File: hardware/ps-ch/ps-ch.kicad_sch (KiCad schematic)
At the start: 67 parts, among them Q11 MMBT3904, U10 ADuM1401xRW, U11 LMR51610X, U13 ADuM1401xRW, U3 LM61495, U5 OPA992IDCKR

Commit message: - added component values/part numbers
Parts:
- removed C24, C33, C41, C50, C51, C52, C53, C57, C61: C, symbol Device:C
- removed R20: R, symbol Device:R
- added C24, C50, C52, C53, C57, C81: 0.1μF 0603 100Vdc X7R ±20%, Capacitor_SMD:C_0603_1608Metric, symbol ps-ch:0.1μF 0603 100Vdc X7R ±20%
- added C33, C41: 10μF 0805 50Vdc X5R ±20%, Capacitor_SMD:C_0805_2012Metric, symbol ps-ch:10μF 0805 50Vdc X5R ±20%
- added C51, C61: 10μF 1210 100Vdc X7S ±20%, Capacitor_SMD:C_1210_3225Metric, symbol ps-ch:10μF 1210 100Vdc X7S ±20%
- C12, C20, C21, C22: value C -> 10μF 1210 100Vdc X7S ±20%; footprint (none) -> Capacitor_SMD:C_1210_3225Metric; symbol Device:C -> ps-ch:10μF 1210 100Vdc X7S ±20%; DisplayValue0 (none) -> 10μF ±20%; DisplayValue1 (none) -> 1210 100Vdc; DisplayValue2 (none) -> X7S; Manufacturer (none) -> Murata; Manufacturer Part Number (none) -> GRM188R72A104MA35
- C14, C19, C23, C34, C46, C47, C48, C56: value C -> 0.1μF 0603 100Vdc X7R ±20%; footprint (none) -> Capacitor_SMD:C_0603_1608Metric; symbol Device:C -> ps-ch:0.1μF 0603 100Vdc X7R ±20%; DisplayValue0 (none) -> 0.1μF ±20%; DisplayValue1 (none) -> 0603 100Vdc; DisplayValue2 (none) -> X7R; Manufacturer (none) -> Murata; Manufacturer Part Number (none) -> GRM188R72A104MA35
- L4: value L -> 60Ω@100MHz; footprint (none) -> Inductor_SMD:L_0603_1608Metric; symbol Device:L -> ps-ch:74437349015; Manufacturer (none) -> Wuerth Elektronik; Manufacturer Part Number (none) -> 74279228600
- R50, R56, R63, R67: value R -> 10kΩ 0603 0.1W ±1% ±100ppm/°C; footprint (none) -> Resistor_SMD:R_0603_1608Metric; symbol Device:R -> ps-ch:10kΩ 0603 0.1W ±1% ±100ppm/°C; DisplayValue0 (none) -> 10kΩ ±1%; DisplayValue1 (none) -> 0603 0.1W; DisplayValue2 (none) -> ±100ppm; Manufacturer (none) -> Yageo; Manufacturer Part Number (none) -> AC0603FR-0710KL
- R57, R58: value R -> 22Ω 0402 0.063W ±1% ±100ppm/°C; footprint (none) -> Resistor_SMD:R_0402_1005Metric; symbol Device:R -> ps-ch:22Ω 0402 0.063W ±1% ±100ppm/°C; DisplayValue0 (none) -> 22Ω ±1%; DisplayValue1 (none) -> 0402 0.063W; DisplayValue2 (none) -> ±100ppm; Manufacturer (none) -> Yageo; Manufacturer Part Number (none) -> AC0402FR-0722RL
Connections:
- net +3V3: now also C19.2, C46.2, R50.1, C52.2, C53.2, C57.2, C81.2; no longer C19.1, C46.1, R50.2
- net 3V3: now also C47.2, C56.2, R56.2; no longer C47.1, C56.1, R56.1
- net ACTIVATE_BOOTLOADER: now also R63.2; no longer R63.1
- net ARM_OUTPUT: now also R67.2; no longer R67.1
- net Earth: now also C47.1, C56.1, R63.1, R67.1; no longer C47.2, C56.2, R63.2, R67.2
- net Flyback Converter/V_PREREG_EQUIV_PWM: now also U10.14 (VOA)
- net GND: now also C12.1, C19.1, C20.1, C21.1, C22.1, C23.1, C34.1, C46.1, C24.1, C33.1, C41.1, C50.1, C51.1, C52.1, C53.1, C57.1, C61.1, C81.1; no longer C12.2, C19.2, C20.2, C21.2, C22.2, C23.2, C34.2, C46.2
- net NRST: now also R56.1; no longer R56.2
- net PG: now also R50.2; no longer R50.1
- net STM32/STM32_UART_RX: now also R58.2; no longer R58.1
- net UART_RX: now also R57.1; no longer R57.2
- net VDC: now also L4.2, C41.2, C61.2; no longer L4.1
- net at L2.1, U3.16 (SW): now also C14.2; no longer C14.1
- net at U13.6 (VOD): now also R57.2; no longer R57.1
- net at L6.2, U11.4 (EN), U11.5 (VIN): now also C50.2, C51.2
- net at R9.1, U3.4 (CBOOT): now also C14.1; no longer C14.2
- net at U11.1 (CB): now also C48.1; no longer C48.2
- net at L5.1, U11.6 (SW): now also C48.2; no longer C48.1
- net at U13.12 (VOC): now also R58.1; no longer R58.2
- new net: C12.2, C20.2, C21.2, C22.2, C23.2, C24.2, L1.2, U3.14 (VIN1), U3.2 (VIN2)
- new net: C33.2, C34.2, L4.1, U5.5 (V+)
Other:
- note added: "0R"

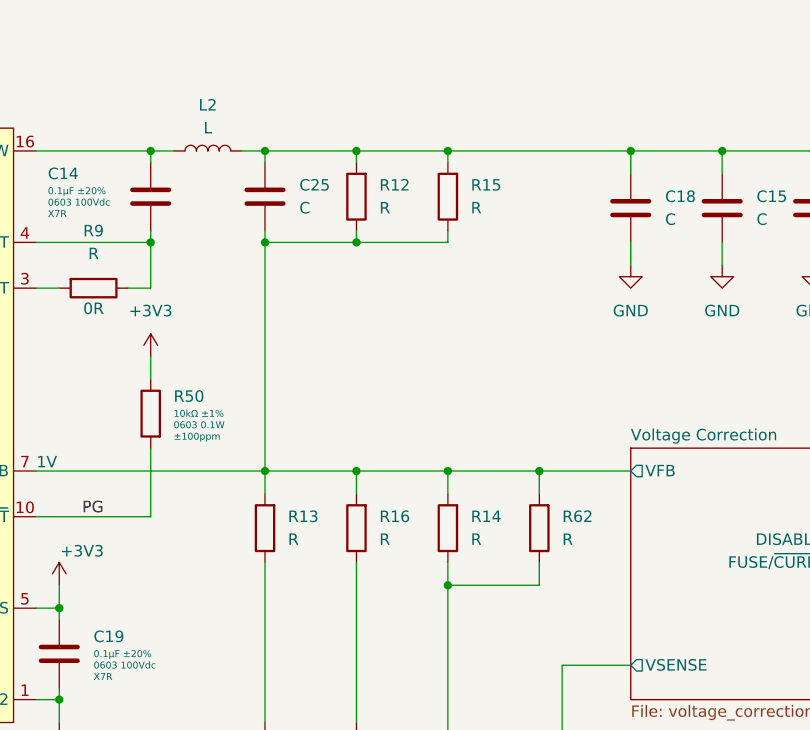
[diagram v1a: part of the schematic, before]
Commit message: calculated voltage dividers
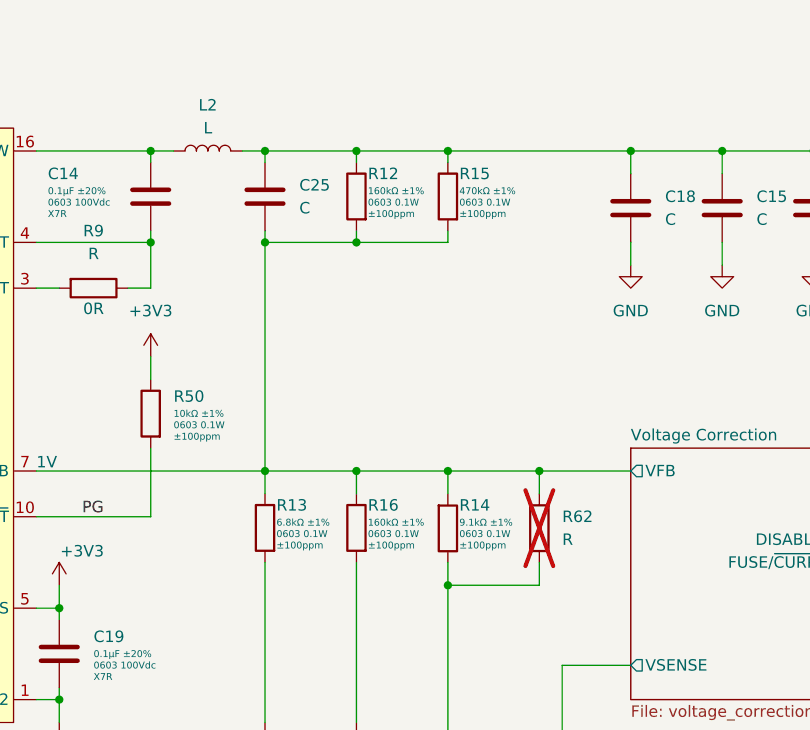
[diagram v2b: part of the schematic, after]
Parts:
- removed R14: R, symbol Device:R
- added R14: 22Ω 0402 0.063W ±1% ±100ppm/°C, Resistor_SMD:R_0603_1608Metric, symbol ps-ch:9.1kΩ 0603 0.1W ±1% ±100ppm/°C
- R12, R16: value R -> 160kΩ 0603 0.1W ±1% ±100ppm/°C; footprint (none) -> Resistor_SMD:R_0603_1608Metric; symbol Device:R -> ps-ch:160kΩ 0603 0.1W ±1% ±100ppm/°C; DisplayValue0 (none) -> 160kΩ ±1%; DisplayValue1 (none) -> 0603 0.1W; DisplayValue2 (none) -> ±100ppm; Manufacturer (none) -> Yageo; Manufacturer Part Number (none) -> AC0603FR-07160kL
- R13: value R -> 6.8kΩ 0603 0.1W ±1% ±100ppm/°C; footprint (none) -> Resistor_SMD:R_0603_1608Metric; symbol Device:R -> ps-ch:6.8kΩ 0603 0.1W ±1% ±100ppm/°C; DisplayValue0 (none) -> 6.8kΩ ±1%; DisplayValue1 (none) -> 0603 0.1W; DisplayValue2 (none) -> ±100ppm; Manufacturer (none) -> Yageo; Manufacturer Part Number (none) -> AC0603FR-076k8L
- R15: value R -> 470kΩ 0603 0.1W ±1% ±100ppm/°C; footprint (none) -> Resistor_SMD:R_0603_1608Metric; symbol Device:R -> ps-ch:470kΩ 0603 0.1W ±1% ±100ppm/°C; DisplayValue0 (none) -> 470kΩ ±1%; DisplayValue1 (none) -> 0603 0.1W; DisplayValue2 (none) -> ±100ppm; Manufacturer (none) -> Yageo; Manufacturer Part Number (none) -> AC0603FR-07470kL
- R62: now not fitted
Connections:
- net GND: now also R13.2, R16.2; no longer R13.1, R16.1
- net Voltage Correction/VFB: now also R12.2, R13.1, R15.2, R16.1, R14.2; no longer R12.1, R13.2, R15.1, R16.2
- net at C15.1, C16.1, C17.1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: now also R12.1, R15.1; no longer R12.2, R15.2
- net at R62.1, U5.3 (-), U5.4: now also R14.1

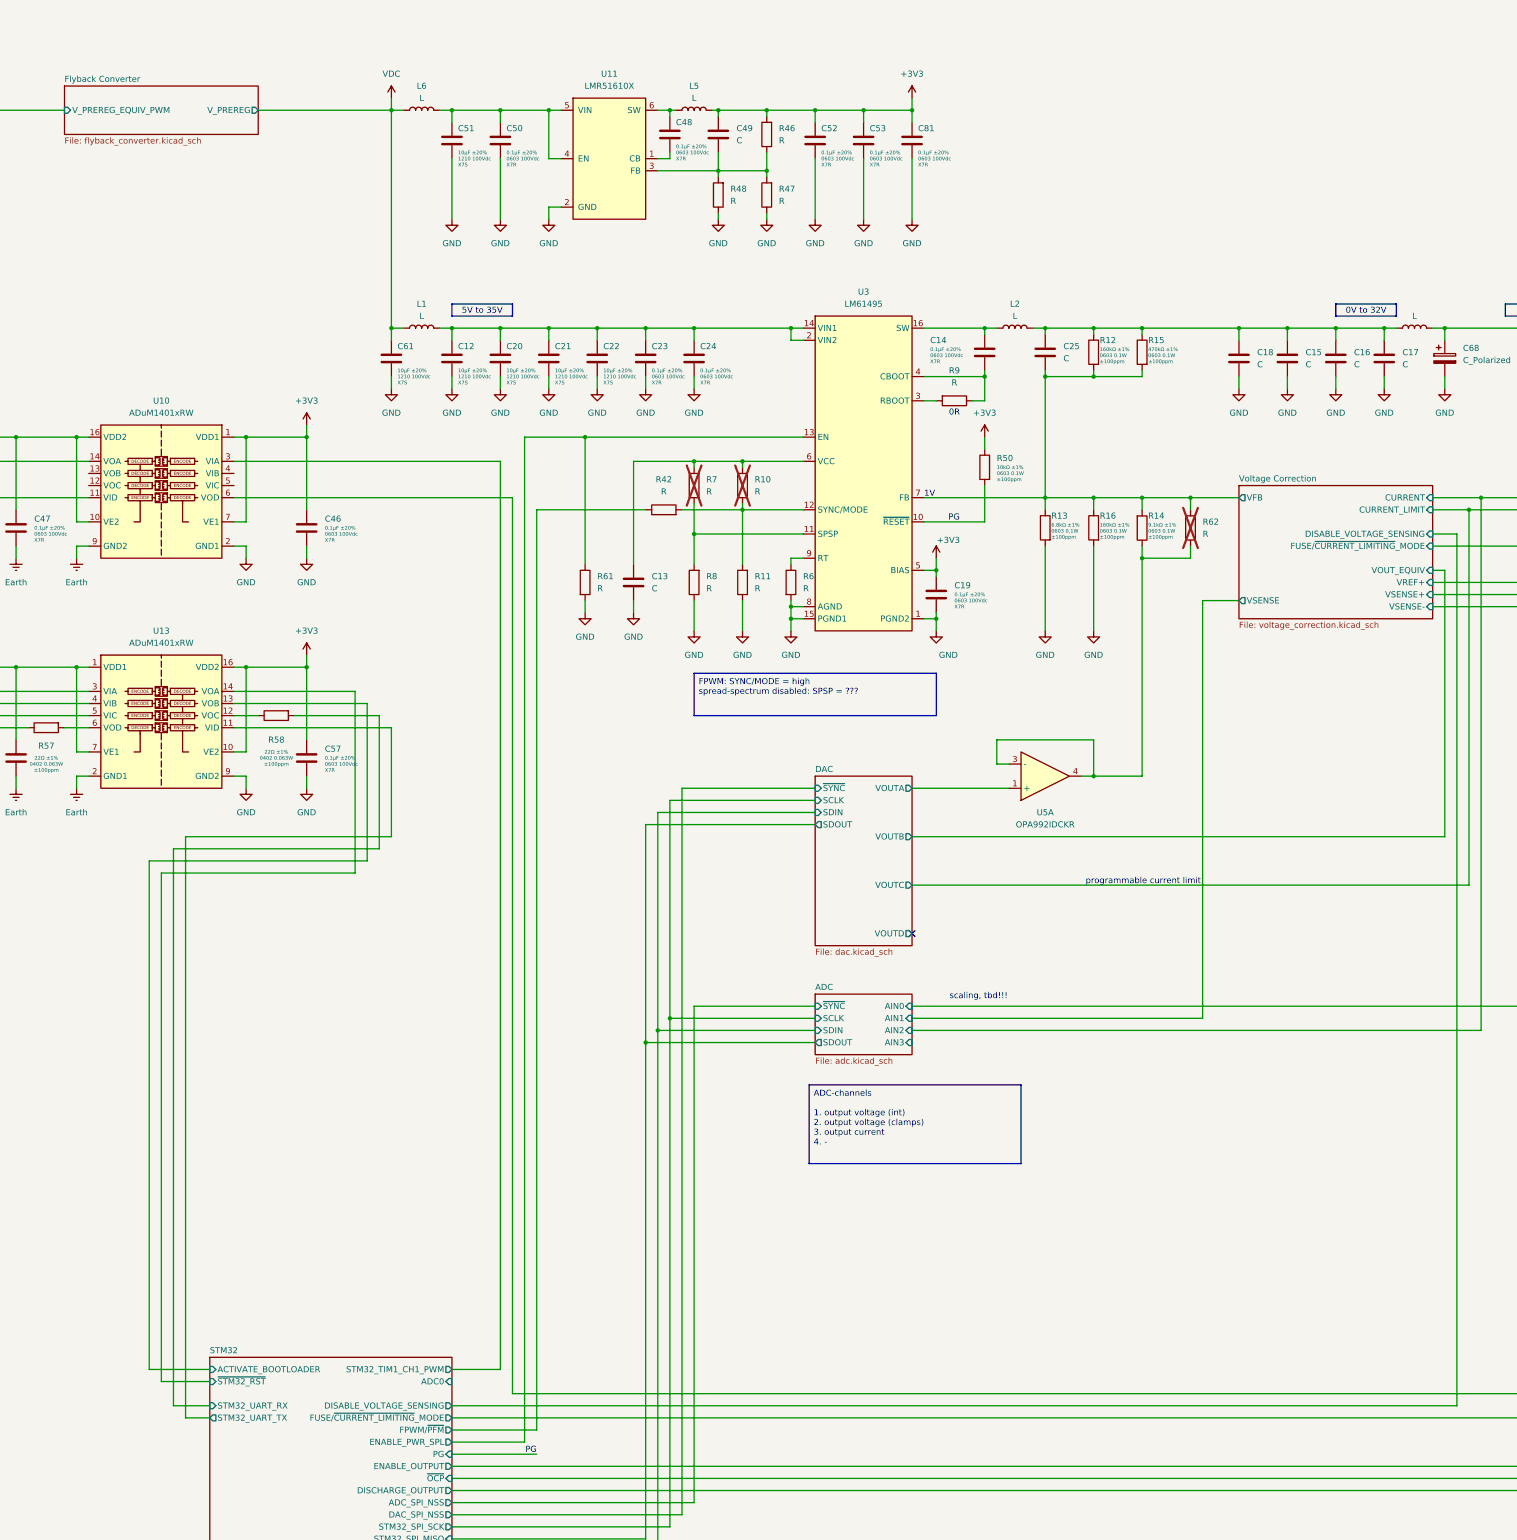
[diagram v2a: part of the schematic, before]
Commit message: added calculations and component values
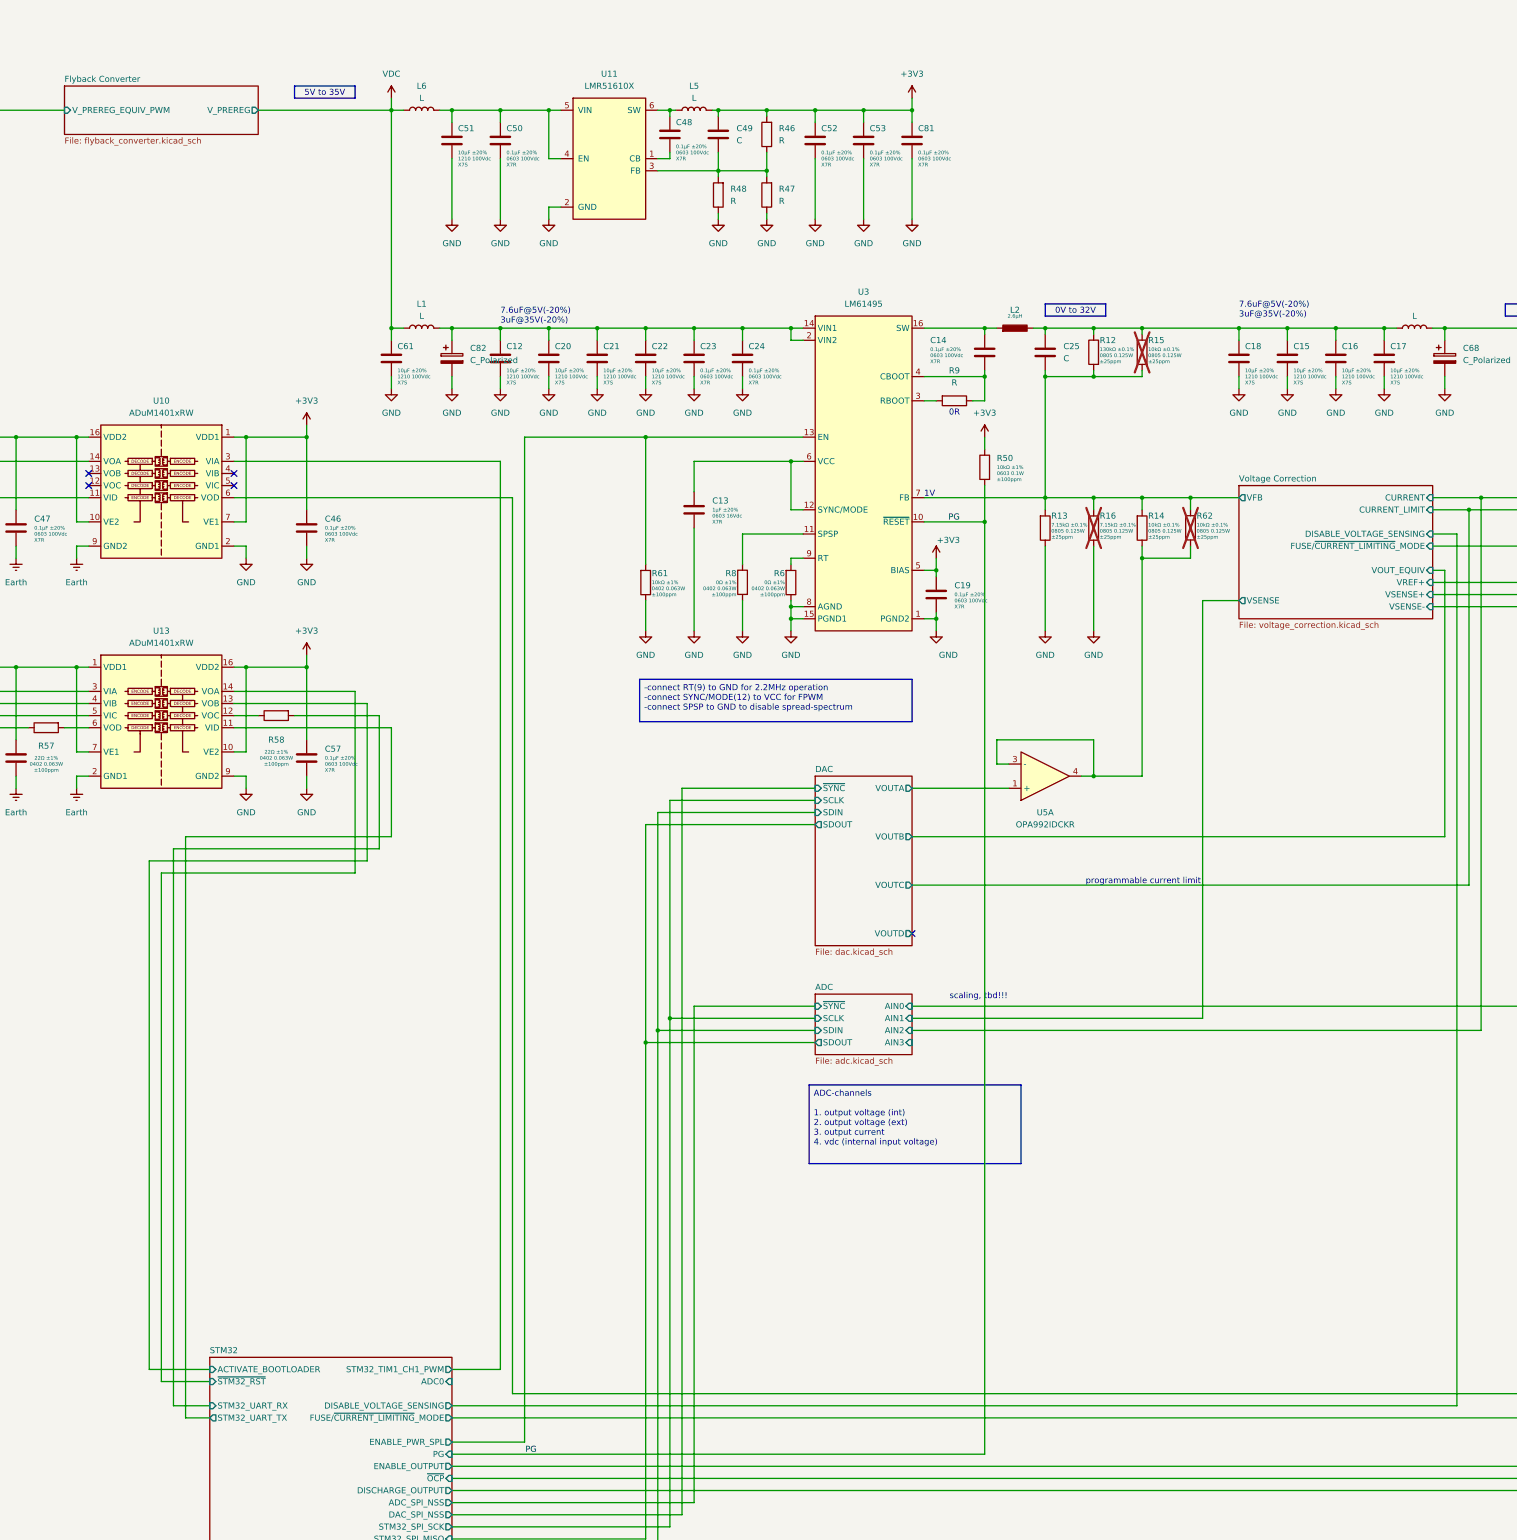
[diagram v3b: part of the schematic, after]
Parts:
- removed C15, C16, C17, C18: C, symbol Device:C
- removed L2: L, symbol Device:L
- removed R10, R11, R42, R7: R, symbol Device:R
- added C15, C16, C17, C18: 10μF 1210 100Vdc X7S ±20%, Capacitor_SMD:C_1210_3225Metric, symbol ps-ch:10μF 1210 100Vdc X7S ±20%
- added C82: C_Polarized, symbol Device:C_Polarized
- added L2: 2.6µH, symbol ps-ch:7443556260
- C12, C20, C21, C22, C51, C61: Manufacturer Part Number GRM188R72A104MA35 -> GRM32EC72A106ME05
- C13: value C -> 1μF 0603 16Vdc X7R ±20%; footprint (none) -> Capacitor_SMD:C_0603_1608Metric; symbol Device:C -> ps-ch:1μF 0603 16Vdc X7R ±20%; DisplayValue0 (none) -> 1μF ±20%; DisplayValue1 (none) -> 0603 16Vdc; DisplayValue2 (none) -> X7R; Manufacturer (none) -> Murata; Manufacturer Part Number (none) -> GCM188R71C105MA49
- R12: value 160kΩ 0603 0.1W ±1% ±100ppm/°C -> 130kΩ 0805 0.125W ±0.1% ±25ppm/°C; footprint Resistor_SMD:R_0603_1608Metric -> Resistor_SMD:R_0805_2012Metric; symbol ps-ch:160kΩ 0603 0.1W ±1% ±100ppm/°C -> ps-ch:130kΩ 0805 0.125W ±0.1% ±25ppm/°C; DisplayValue0 160kΩ ±1% -> 130kΩ ±0.1%; DisplayValue1 0603 0.1W -> 0805 0.125W; DisplayValue2 ±100ppm -> ±25ppm; Manufacturer Part Number AC0603FR-07160kL -> RT0805BRD07130KL
- R13: value 6.8kΩ 0603 0.1W ±1% ±100ppm/°C -> 7.15kΩ 0805 0.125W ±0.1% ±25ppm/°C; footprint Resistor_SMD:R_0603_1608Metric -> Resistor_SMD:R_0805_2012Metric; symbol ps-ch:6.8kΩ 0603 0.1W ±1% ±100ppm/°C -> ps-ch:7.15kΩ 0805 0.125W ±0.1% ±25ppm/°C; DisplayValue0 6.8kΩ ±1% -> 7.15kΩ ±0.1%; DisplayValue1 0603 0.1W -> 0805 0.125W; DisplayValue2 ±100ppm -> ±25ppm; Manufacturer Part Number AC0603FR-076k8L -> RT0805BRD077K15L
- R14: value 22Ω 0402 0.063W ±1% ±100ppm/°C -> 10kΩ 0805 0.125W ±0.1% ±25ppm/°C; footprint Resistor_SMD:R_0603_1608Metric -> Resistor_SMD:R_0805_2012Metric; symbol ps-ch:9.1kΩ 0603 0.1W ±1% ±100ppm/°C -> ps-ch:10kΩ 0805 0.125W ±0.1% ±25ppm/°C; DisplayValue0 9.1kΩ ±1% -> 10kΩ ±0.1%; DisplayValue1 0603 0.1W -> 0805 0.125W; DisplayValue2 ±100ppm -> ±25ppm; Manufacturer Part Number AC0603FR-079K1L -> RT0805BRD0710KL
- R15: value 470kΩ 0603 0.1W ±1% ±100ppm/°C -> 10kΩ 0805 0.125W ±0.1% ±25ppm/°C; footprint Resistor_SMD:R_0603_1608Metric -> Resistor_SMD:R_0805_2012Metric; symbol ps-ch:470kΩ 0603 0.1W ±1% ±100ppm/°C -> ps-ch:10kΩ 0805 0.125W ±0.1% ±25ppm/°C; DisplayValue0 470kΩ ±1% -> 10kΩ ±0.1%; DisplayValue1 0603 0.1W -> 0805 0.125W; DisplayValue2 ±100ppm -> ±25ppm; Manufacturer Part Number AC0603FR-07470kL -> RT0805BRD0710KL; now not fitted
- R16: value 160kΩ 0603 0.1W ±1% ±100ppm/°C -> 7.15kΩ 0805 0.125W ±0.1% ±25ppm/°C; footprint Resistor_SMD:R_0603_1608Metric -> Resistor_SMD:R_0805_2012Metric; symbol ps-ch:160kΩ 0603 0.1W ±1% ±100ppm/°C -> ps-ch:7.15kΩ 0805 0.125W ±0.1% ±25ppm/°C; DisplayValue0 160kΩ ±1% -> 7.15kΩ ±0.1%; DisplayValue1 0603 0.1W -> 0805 0.125W; DisplayValue2 ±100ppm -> ±25ppm; Manufacturer Part Number AC0603FR-07160kL -> RT0805BRD077K15L; now not fitted
- R6, R8: value R -> 0Ω 0402 0.063W ±1% ±100ppm/°C; footprint (none) -> Resistor_SMD:R_0402_1005Metric; symbol Device:R -> ps-ch:0Ω 0402 0.063W ±1% ±100ppm/°C; DisplayValue0 (none) -> 0Ω ±1%; DisplayValue1 (none) -> 0402 0.063W; DisplayValue2 (none) -> ±100ppm; Manufacturer (none) -> Yageo; Manufacturer Part Number (none) -> AC0402FR-070RL
- R61: value R -> 10kΩ 0402 0.063W ±1% ±100ppm/°C; footprint (none) -> Resistor_SMD:R_0402_1005Metric; symbol Device:R -> ps-ch:10kΩ 0402 0.063W ±1% ±100ppm/°C; DisplayValue0 (none) -> 10kΩ ±1%; DisplayValue1 (none) -> 0402 0.063W; DisplayValue2 (none) -> ±100ppm; Manufacturer (none) -> Yageo; Manufacturer Part Number (none) -> AC0402FR-0710KL
- R62: value R -> 10kΩ 0805 0.125W ±0.1% ±25ppm/°C; footprint (none) -> Resistor_SMD:R_0805_2012Metric; symbol Device:R -> ps-ch:10kΩ 0805 0.125W ±0.1% ±25ppm/°C; DisplayValue0 (none) -> 10kΩ ±0.1%; DisplayValue1 (none) -> 0805 0.125W; DisplayValue2 (none) -> ±25ppm; Manufacturer (none) -> Yageo; Manufacturer Part Number (none) -> RT0805BRD0710KL
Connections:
- net GND: now also C13.1, R13.1, R16.1, R6.1, R61.1, R8.2, C15.1, C16.1, C17.1, C18.1, C82.2; no longer C13.2, R13.2, R16.2, R6.2, R61.2, R8.1
- net STM32/ENABLE_PWR_SPL: now also R61.2; no longer R61.1
- net Voltage Correction/VFB: now also R13.2, R16.2, R62.1; no longer R13.1, R16.1, R62.2
- net at C12.2, C20.2, C21.2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: now also C82.1
- net at U3.12 (SYNC/MODE): now also C13.2, U3.6 (VCC)
- net at C25.1, L9.1, R12.1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: now also C15.2, C16.2, C17.2, C18.2, L2.1
- net at C14.2, U3.16 (SW): now also L2.2
- net at U3.11 (SPSP): now also R8.1; no longer R8.2
- net at R14.1, U5.3 (-), U5.4: now also R62.2; no longer R62.1
- net at U3.9 (RT): now also R6.2; no longer R6.1
- no-connect marks 1 -> 5
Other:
- sheet STM32 ports: added none; removed FPWM/~{PFM}
- note added: "7.6uF@5V(-20%) 3uF@35V(-20%)"
- moved on the sheet: C12, C13, C20, C21, C22, C23, C24, R13, R61, R8
